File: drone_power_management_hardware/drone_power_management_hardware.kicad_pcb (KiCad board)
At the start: 2 copper layers, 29.4 x 23 mm, 31 parts

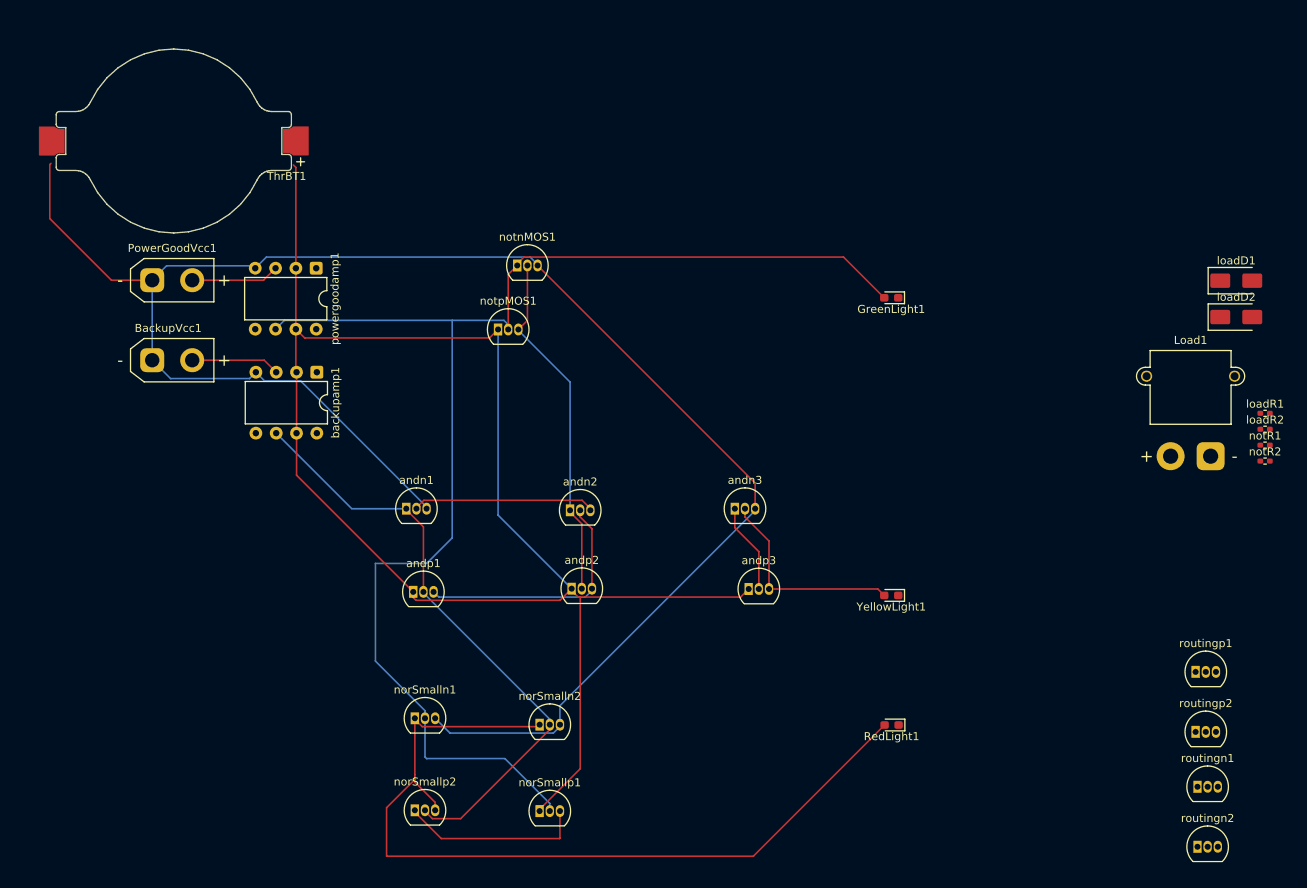
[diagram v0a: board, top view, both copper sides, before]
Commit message: Connected all remaining components on pcb
- cut board size
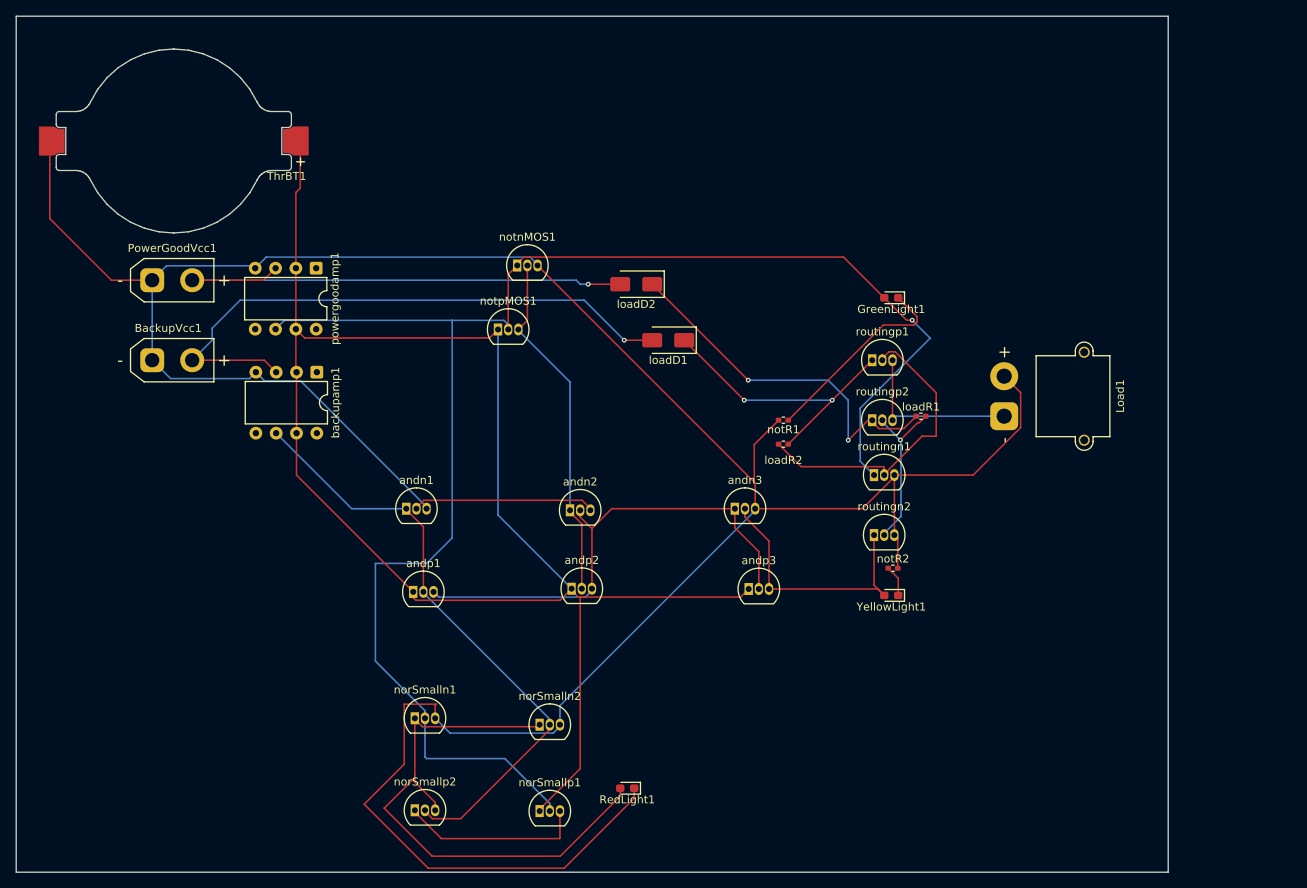
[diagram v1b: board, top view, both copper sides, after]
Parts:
- moved loadD2 75.1 mm to (94.0, 52.5), turned to 180 degrees
- moved loadD1 71.4 mm to (98.0, 59.5), turned to 180 degrees
- moved notR1 60.3 mm to (112.4, 69.5), turned to 180 degrees
- moved loadR2 60.2 mm to (112.4, 72.5)
- moved routingp1 56.1 mm to (123.5, 62.0)
- moved routingp2 56.1 mm to (123.5, 69.5)
- moved routingn1 56.1 mm to (123.7, 76.4)
- moved routingn2 56.1 mm to (123.7, 83.9)
- moved notR2 48.4 mm to (126.1, 88.0)
- moved loadR1 43.0 mm to (129.6, 69.0)
- moved RedLight1 34.0 mm to (92.9, 115.5)
- moved Load1 26.3 mm to (140.0, 69.0), turned to -90 degrees
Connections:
- routingn2 pad 1: andOutput -> andOut
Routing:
- net Ground: track 221.6 -> 352.5 mm
- net POWER_GOOD_BACKUP: track 11.1 -> 74.7 mm, vias 0 -> 1
- net POWER_GOOD: track 11.0 -> 64.7 mm, vias 0 -> 1
- net Net-(loadD2-K): track 0.00 -> 46.2 mm, vias 0 -> 2
- net Net-(routingn1-D): track 0.00 -> 39.0 mm
- net norSmallp2 out: track 108.9 -> 70.2 mm
- net Net-(loadD1-K): track 0.00 -> 36.5 mm, vias 0 -> 2
- net goodAmpOut: track 171.2 -> 200.5 mm, vias 0 -> 1
- net Net-(GreenLight1-K): track 0.00 -> 25.2 mm
- net motorPower: track 0.00 -> 22.7 mm
- net Net-(routingn2-D): track 0.00 -> 21.2 mm, vias 0 -> 1
- net andDrain: track 42.3 -> 61.2 mm
- net andOut: track 26.0 -> 34.1 mm
- net Net-(YellowLight1-K): track 0.00 -> 3.92 mm
- net 3.2v power: track 195.2 -> 198.4 mm
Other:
- board size 29.4 x 23 mm -> 144 x 107 mm

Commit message: Moved nor gate
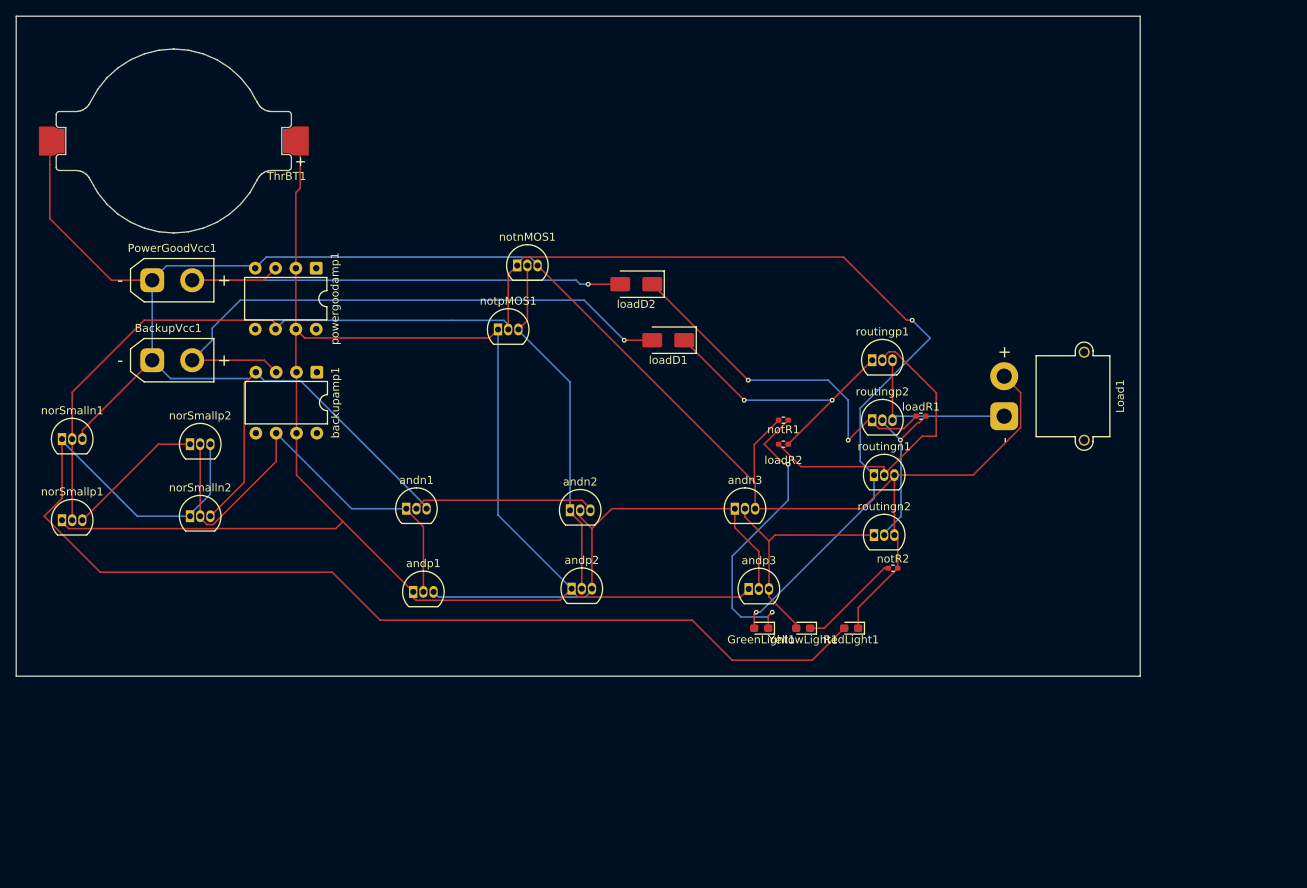
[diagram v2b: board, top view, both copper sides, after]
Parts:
- moved norSmallp1 69.9 mm to (22.2, 82.0)
- moved norSmalln1 56.2 mm to (22.2, 71.9)
- moved norSmallp2 53.7 mm to (38.2, 72.5)
- moved norSmalln2 50.9 mm to (38.2, 81.5)
- moved GreenLight1 44.4 mm to (109.6, 95.5)
- moved RedLight1 34.4 mm to (120.9, 95.5)
- moved YellowLight1 11.7 mm to (114.9, 95.5)
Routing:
- net norSmallp2 out: track 70.2 -> 149.9 mm
- net Ground: track 352.5 -> 279.7 mm
- net backupAmpOut: track 75.9 -> 57.5 mm
- net goodAmpOut: track 200.5 -> 188.3 mm, vias 1 -> 2
- net Net-(GreenLight1-K): track 25.2 -> 37.1 mm, vias 0 -> 2
- net Net-(YellowLight1-K): track 3.92 -> 12.9 mm
- net 3.2v power: track 198.4 -> 205.6 mm
- net Net-(norSmallp1-D): track 23.1 -> 17.4 mm
- net andOut: track 34.1 -> 31.0 mm
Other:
- board size 144 x 107 mm -> 140.5 x 82.5 mm
